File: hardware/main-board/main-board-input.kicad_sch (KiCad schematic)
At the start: 39 parts, among them J5 Conn_01x02, SW1 SW_Push_Long, SW10 SW_Push, SW11 Rotary_Encoder_Switch, SW2 SW_Push_Long, SW3 SW_Push, SW4 SW_Push, SW5 SW_Push, SW6 SW_Push, SW7 SW_Push, SW8 SW_Push, SW9 SW_Push, U6 TCA8418, U7 STP16CPC26

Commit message: Route reset signal to keypad IC
This makes it possible to reset the keypad controller to start up in a
more clean state.

Also adjusted a few via sizes, more in a future commit.

Fix #73
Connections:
- net KEY_~{RES}: now reaches R9.2, U6.20 (~{RESET})
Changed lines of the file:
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@@
+	)
+	(junction
+		(at 40.64 105.41)
+		(diameter 0)
+		(color 0 0 0 0)
 	)
 	(junction
@@
 	(wire
 		(pts
+			(xy 29.21 105.41) (xy 40.64 105.41)
+		)
+		(stroke
+			(width 0)
+			(type default)
+		)
+	)
+	(wire
+		(pts
 			(xy 76.2 119.38) (xy 83.82 119.38)
 		)
@@
 		(fields_autoplaced yes)
 		(effects
+			(font
+				(size 1.27 1.27)
+			)
+			(justify right)
+		)
+	)
+	(hierarchical_label "KEY_~{RES}"
+		(shape input)
+		(at 29.21 105.41 180)
+		(fields_autoplaced yes)
+		(effects

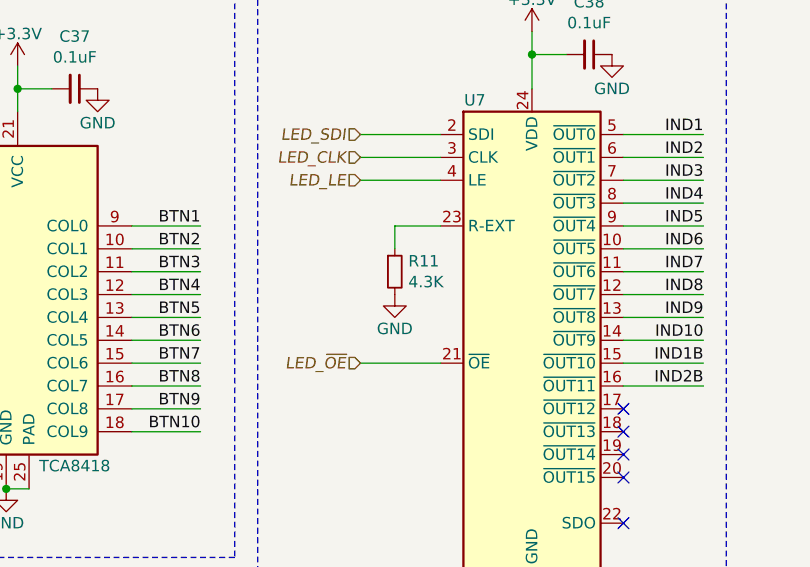
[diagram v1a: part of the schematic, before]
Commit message: Fix labeling of 1% resistors
This just affected two components, but the review was necessary.

Fix #71
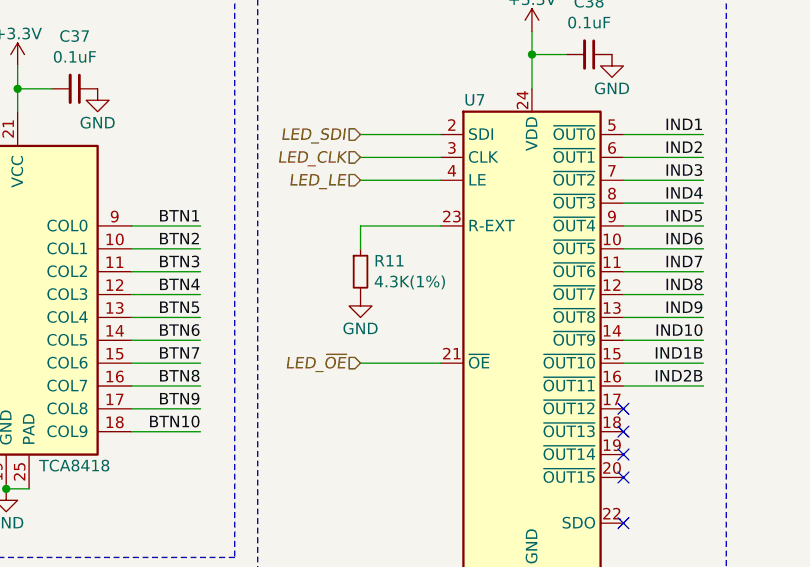
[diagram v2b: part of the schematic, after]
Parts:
- R11: value 4.3K -> 4.3K(1%)
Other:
- moved on the sheet: R11
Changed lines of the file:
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@@
 	(wire
 		(pts
-			(xy 110.49 104.14) (xy 105.41 104.14)
+			(xy 110.49 104.14) (xy 101.6 104.14)
 		)
 		(stroke
@@
 	(wire
 		(pts
-			(xy 105.41 104.14) (xy 105.41 106.68)
+			(xy 101.6 104.14) (xy 101.6 106.68)
 		)
 		(stroke
@@
 	(symbol
 		(lib_id "Device:R_Small")
-		(at 105.41 109.22 0)
+		(at 101.6 109.22 0)
 		(unit 1)
 		(exclude_from_sim no)
@@
 		(dnp no)
 		(property "Reference" "R11"
-			(at 106.9086 108.0516 0)
+			(at 103.0986 108.0516 0)
 			(effects
 				(font
@@
 			)
 		)
-		(property "Value" "4.3K"
-			(at 106.9086 110.363 0)
+		(property "Value" "4.3K(1%)"
+			(at 103.0986 110.363 0)
 			(effects
 				(font
@@
 		)
 		(property "Footprint" "Resistor_SMD:R_0603_1608Metric"
-			(at 105.41 109.22 0)
+			(at 101.6 109.22 0)
 			(effects
 				(font
@@
 		)
 		(property "Datasheet" "https://www.vishay.com/docs/20035/dcrcwe3.pdf"
-			(at 105.41 109.22 0)
+			(at 101.6 109.22 0)
 			(effects
 				(font
@@
 		)
 		(property "Description" "RES SMD 4.3K OHM 1% 1/10W 0603"
-			(at 105.41 109.22 0)
+			(at 101.6 109.22 0)
 			(effects
 				(font
@@
 		)
 		(property "Manufacturer" "Vishay Dale"
-			(at 105.41 109.22 0)
+			(at 101.6 109.22 0)
 			(effects
 				(font
@@
 		)
 		(property "Manufacturer PN" "CRCW06034K30FKEA"
-			(at 105.41 109.22 0)
+			(at 101.6 109.22 0)
 			(effects
 				(font
@@
 		)
 		(property "Supplier" "Digi-Key"
-			(at 105.41 109.22 0)
+			(at 101.6 109.22 0)
 			(effects
 				(font
@@
 		)
 		(property "Supplier PN" "541-4.30KHCT-ND"
-			(at 105.41 109.22 0)
+			(at 101.6 109.22 0)
 			(effects
 				(font
@@
 	(symbol
 		(lib_id "power:GND")
-		(at 105.41 111.76 0)
+		(at 101.6 111.76 0)
 		(unit 1)
 		(exclude_from_sim no)
@@
 		(dnp no)
 		(property "Reference" "#PWR081"
-			(at 105.41 118.11 0)
+			(at 101.6 118.11 0)
 			(effects
 				(font
@@
 		)
 		(property "Value" "GND"
-			(at 105.41 115.57 0)
+			(at 101.6 115.57 0)
 			(effects
 				(font
@@
 		)
 		(property "Footprint" ""
-			(at 105.41 111.76 0)
+			(at 101.6 111.76 0)
 			(effects
 				(font
@@
 		)
 		(property "Datasheet" ""
-			(at 105.41 111.76 0)
+			(at 101.6 111.76 0)
 			(effects
 				(font
@@
 		)
 		(property "Description" "Power symbol creates a global label with name \"GND\" , ground"
-			(at 105.41 111.76 0)
+			(at 101.6 111.76 0)
 			(effects
 				(font

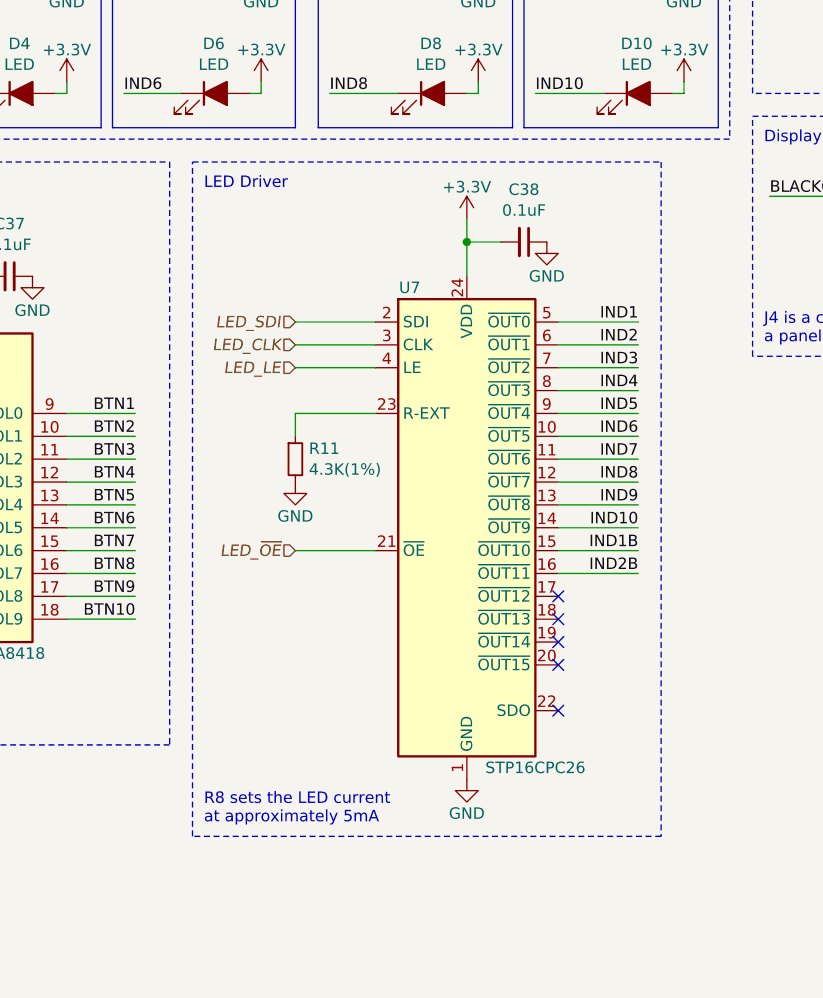
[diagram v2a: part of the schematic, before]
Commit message: Swap LED driver from STP16CPC26 to AW9523B
This update involves both the schematic and PCB layout changes to switch
to a different LED driver. The new driver is simpler to operate (I2C vs
SPI and supplemental signals), cheaper, and supports per-LED dimming
control.

The hardware reset line was still routed, despite it being technically
unnecessary, to help ensure that the IC always comes up in a clean state
before the MCU has a chance to talk to it.

Fix #77
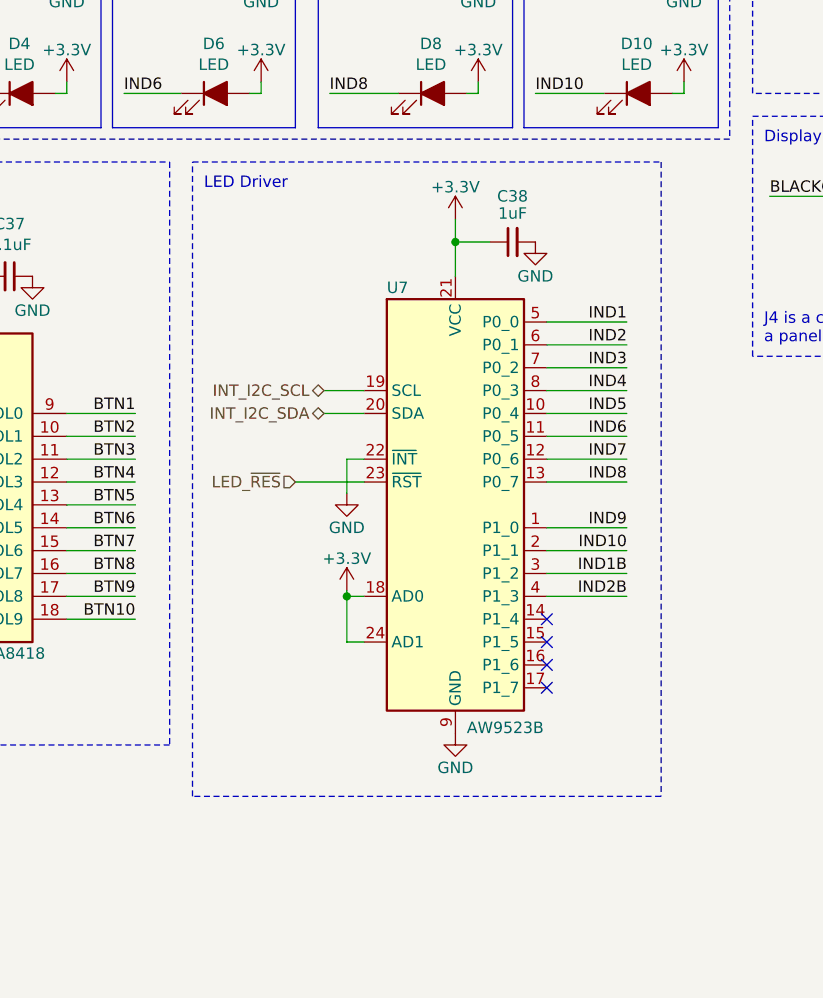
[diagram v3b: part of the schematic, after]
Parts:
- removed R11: 4.3K(1%), Resistor_SMD:R_0603_1608Metric, symbol Device:R_Small
- removed U7: STP16CPC26, Package_SO:QSOP-24_3.9x8.7mm_P0.635mm, symbol Project:STP16CPC26
- added U7: AW9523B, Package_DFN_QFN:QFN-24-1EP_4x4mm_P0.5mm_EP2.7x2.7mm, symbol Interface_Expansion:AW9523B
- C38: value 0.1uF -> 1uF; Manufacturer PN CL10B104KA8NNNC -> CL10B105KA8NNNC; Supplier PN 1276-1006-1-ND -> 1276-1184-1-ND
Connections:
- net +3.3V: now also C38.1, U7.18 (AD0), U7.21 (VCC), U7.24 (AD1); no longer C38.2
- net GND: now also C38.2, U7.22 (~{INT}), U7.25 (GND), U7.9 (GND); no longer C38.1
- net IND1: now also U7.5 (P0_0)
- net IND10: now also U7.2 (P1_1)
- net IND1B: now also U7.3 (P1_2)
- net IND2: now also U7.6 (P0_1)
- net IND2B: now also U7.4 (P1_3)
- net IND3: now also U7.7 (P0_2)
- net IND4: now also U7.8 (P0_3)
- net IND5: now also U7.10 (P0_4)
- net IND6: now also U7.11 (P0_5)
- net IND7: now also U7.12 (P0_6)
- net IND8: now also U7.13 (P0_7)
- net IND9: now also U7.1 (P1_0)
- net INT_I2C_SCL: now also U7.19 (SCL)
- net INT_I2C_SDA: now also U7.20 (SDA)
- new net LED_~{RES}: U7.23 (~{RST})
- no-connect marks 5 -> 4
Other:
- note removed: "R8 sets the LED current at approximately 5mA"

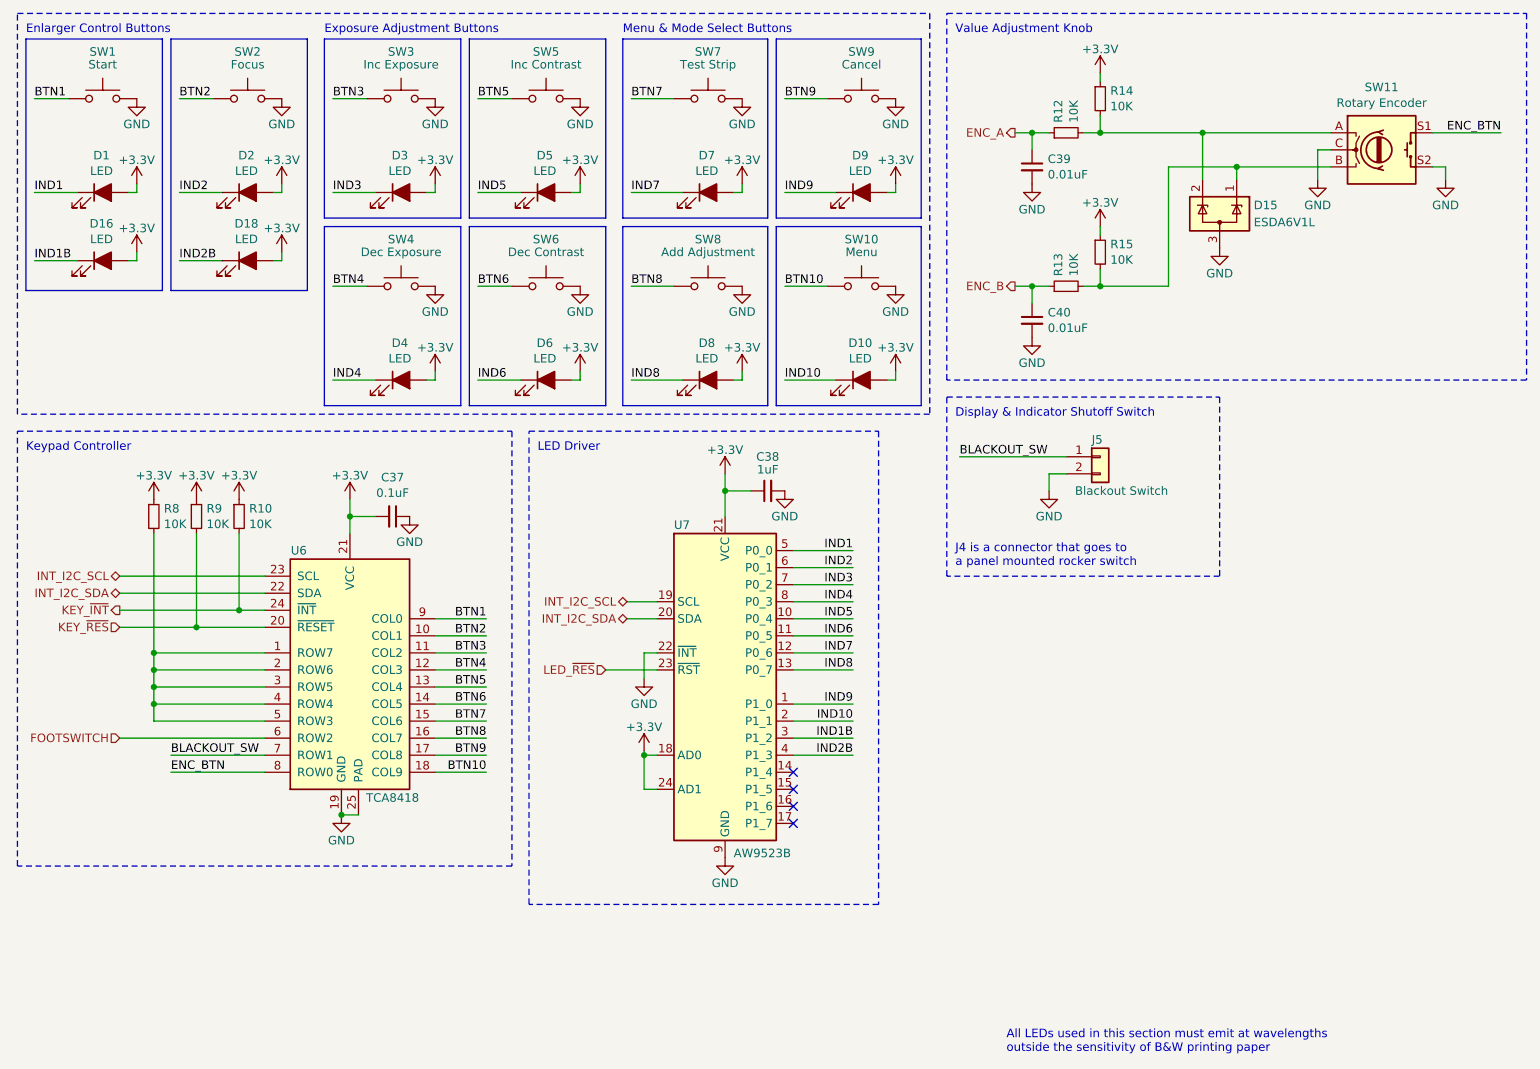
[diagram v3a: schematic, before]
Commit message: Misc schematic cleanup
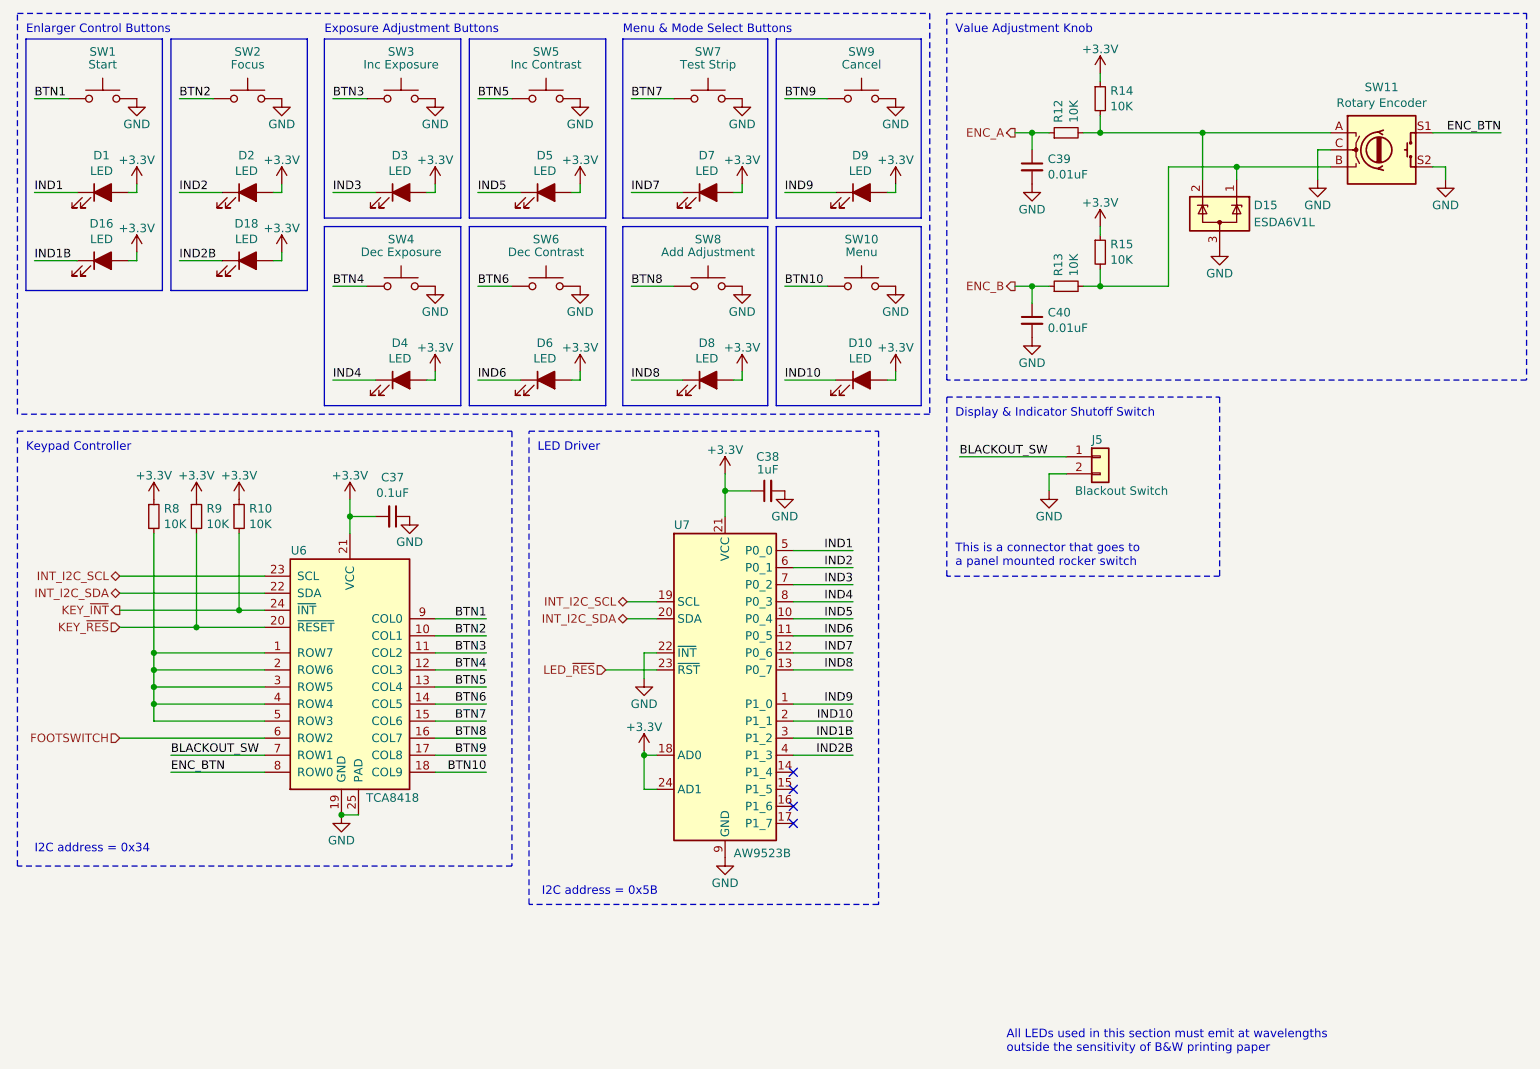
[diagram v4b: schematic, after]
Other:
- note added: "I2C address = 0x34"
- note added: "I2C address = 0x5B"
- note added: "This is a connector that goes to a panel mounted rocker switch"
- note removed: "J4 is a connector that goes to a panel mounted rocker switch"
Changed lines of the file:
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@@
 	(title_block
 		(title "Printalyzer - Main Board (User Input)")
-		(date "2024-04-16")
-		(rev "D")
+		(date "2024-09-01")
+		(rev "F")
 		(company "Dektronics, Inc.")
 		(comment 1 "Derek Konigsberg")
@@
 		)
 	)
-	(text "J4 is a connector that goes to\na panel mounted rocker switch"
+	(text "I2C address = 0x34"
+		(exclude_from_sim no)
+		(at 16.51 138.43 0)
+		(effects
+			(font
+				(size 1.27 1.27)
+			)
+			(justify left)
+		)
+	)
+	(text "This is a connector that goes to\na panel mounted rocker switch"
 		(exclude_from_sim no)
 		(at 153.67 96.52 0)
@@
 		)
 	)
+	(text "I2C address = 0x5B"
+		(exclude_from_sim no)
+		(at 92.075 144.78 0)
+		(effects
+			(font
+				(size 1.27 1.27)
+			)
+			(justify left)
+		)
+	)

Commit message: Update schematic and layout dates and generate images
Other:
- title: Printalyzer - Main Board (User Input) -> Printalyzer - Main Board
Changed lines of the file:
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@@
 	(paper "USLetter")
 	(title_block
-		(title "Printalyzer - Main Board (User Input)")
-		(date "2024-09-01")
+		(title "Printalyzer - Main Board")
+		(date "2024-09-08")
 		(rev "F")
 		(company "Dektronics, Inc.")
